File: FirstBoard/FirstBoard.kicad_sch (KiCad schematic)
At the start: 25 parts, among them J0 Battery, J1 MPU0, J10 MPU9, J11 MPU10, J12 MPU11, J13 MPU12, J14 OPEN, J2 MPU1, J3 MPU2, J4 MPU3, J5 MPU4, J6 MPU5, J7 MPU6, J8 MPU7, J9 MPU8, U1 ESP32-DEVKIT1-V1-JOAO

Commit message: Adding symbols, footprint and first pcb drawing
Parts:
- removed U1: ESP32-DEVKIT1-V1-JOAO, symbol ESP32-DEVKIT-V1:ESP32-DEVKIT1-V1-JOAO
- removed U?: LM2596-Board, symbol TCC_Library:LM2596-Board
- added U1: ESP32-DEVKIT1-V1-JOAO, TCC_FOOTPRINTS:MODULE_ESP32_DEVKIT_V1, symbol TCC_Library:ESP32-DEVKIT1-V1-JOAO
- added U2: LM2596-Board, TCC_FOOTPRINTS:LM2596_Board, symbol TCC_Library:LM2596-Board
- D0, D1, D2: footprint (none) -> Resistor_THT:R_Axial_DIN0204_L3.6mm_D1.6mm_P7.62mm_Horizontal
- J0: footprint (none) -> Connector_PinHeader_2.54mm:PinHeader_1x02_P2.54mm_Vertical
- J1: footprint (none) -> Connector_PinHeader_2.54mm:PinHeader_1x06_P2.54mm_Vertical
- J10, J11, J12, J13, J2, J3, J4, J5, J6, J7, J8, J9: footprint (none) -> Connector_PinHeader_2.54mm:PinHeader_1x05_P2.54mm_Vertical
- J14: footprint (none) -> Connector_PinHeader_2.54mm:PinHeader_2x04_P2.54mm_Vertical
- R0, R1: footprint (none) -> Resistor_THT:R_Axial_DIN0207_L6.3mm_D2.5mm_P10.16mm_Horizontal
- R2: renamed from R1; footprint (none) -> Resistor_THT:R_Axial_DIN0207_L6.3mm_D2.5mm_P10.16mm_Horizontal
- R3: renamed from R2; footprint (none) -> Resistor_THT:R_Axial_DIN0207_L6.3mm_D2.5mm_P10.16mm_Horizontal
- R4: renamed from R3; footprint (none) -> Resistor_THT:R_Axial_DIN0207_L6.3mm_D2.5mm_P10.16mm_Horizontal
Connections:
- net 3v3: now also U1.16 (3.3V), U2.3 (OUT+)
- net AD0_0: now also U1.12 (D12)
- net AD0_1: now also U1.11 (D14)
- net AD0_10: now also U1.21 (D16)
- net AD0_11: now also U1.22 (D17)
- net AD0_12: now also U1.23 (D5)
- net AD0_2: now also U1.10 (D27)
- net AD0_3: now also U1.9 (D26)
- net AD0_4: now also U1.8 (D25)
- net AD0_5: now also U1.7 (D33)
- net AD0_6: now also U1.6 (D32)
- net AD0_7: now also U1.18 (D15)
- net AD0_8: now also U1.19 (D2)
- net AD0_9: now also U1.20 (D4)
- net BAT+: now also U2.1 (IN+)
- net BAT-: now also U2.2 (IN-)
- net D1: now also U1.28 (D1)
- net GND: now also U1.14 (GND), U1.17 (GND), U2.4 (OUT-)
- net INT: now also U1.13 (D13)
- net LED_B: now also U1.27 (D3)
- net LED_G: now also U1.4 (D34)
- net LED_R: now also U1.5 (D25)
- net MISO: now also U1.25 (D19-MISO)
- net MOSI: now also U1.30 (D23-MOSI)
- net SCK: now also U1.24 (D18-SCK)
- net SCL: now also U1.29 (D22-SCL)
- net SDA: now also U1.26 (D21-SDA)
- net at J14.1 (Pin_1): now also U1.15 (VIN)
- net at J14.2 (Pin_2): now also U1.3 (VN)
- net at J14.3 (Pin_3): now also U1.2 (VP)
- net at J14.4 (Pin_4): now also U1.1 (EN)

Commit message: changing layour, adding SD card
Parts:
- removed D2: LED B, Resistor_THT:R_Axial_DIN0204_L3.6mm_D1.6mm_P7.62mm_Horizontal, symbol Device:LED
- removed J10: MPU9, Connector_PinHeader_2.54mm:PinHeader_1x05_P2.54mm_Vertical, symbol Connector_Generic:Conn_01x05
- removed J11: MPU10, Connector_PinHeader_2.54mm:PinHeader_1x05_P2.54mm_Vertical, symbol Connector_Generic:Conn_01x05
- removed J12: MPU11, Connector_PinHeader_2.54mm:PinHeader_1x05_P2.54mm_Vertical, symbol Connector_Generic:Conn_01x05
- removed J13: MPU12, Connector_PinHeader_2.54mm:PinHeader_1x05_P2.54mm_Vertical, symbol Connector_Generic:Conn_01x05
- removed J14: OPEN, Connector_PinHeader_2.54mm:PinHeader_2x04_P2.54mm_Vertical, symbol Connector_Generic:Conn_01x08
- removed J2: MPU1, Connector_PinHeader_2.54mm:PinHeader_1x05_P2.54mm_Vertical, symbol Connector_Generic:Conn_01x05
- removed J3: MPU2, Connector_PinHeader_2.54mm:PinHeader_1x05_P2.54mm_Vertical, symbol Connector_Generic:Conn_01x05
- removed J4: MPU3, Connector_PinHeader_2.54mm:PinHeader_1x05_P2.54mm_Vertical, symbol Connector_Generic:Conn_01x05
- removed J5: MPU4, Connector_PinHeader_2.54mm:PinHeader_1x05_P2.54mm_Vertical, symbol Connector_Generic:Conn_01x05
- removed J6: MPU5, Connector_PinHeader_2.54mm:PinHeader_1x05_P2.54mm_Vertical, symbol Connector_Generic:Conn_01x05
- removed J7: MPU6, Connector_PinHeader_2.54mm:PinHeader_1x05_P2.54mm_Vertical, symbol Connector_Generic:Conn_01x05
- removed J8: MPU7, Connector_PinHeader_2.54mm:PinHeader_1x05_P2.54mm_Vertical, symbol Connector_Generic:Conn_01x05
- removed J9: MPU8, Connector_PinHeader_2.54mm:PinHeader_1x05_P2.54mm_Vertical, symbol Connector_Generic:Conn_01x05
- removed R0, R1: 4k7, Resistor_THT:R_Axial_DIN0207_L6.3mm_D2.5mm_P10.16mm_Horizontal, symbol Device:R
- removed R4: 220R, Resistor_THT:R_Axial_DIN0207_L6.3mm_D2.5mm_P10.16mm_Horizontal, symbol Device:R
- added J10: MPU9, Connector_PinHeader_2.54mm:PinHeader_1x06_P2.54mm_Vertical, symbol Connector_Generic:Conn_01x06
- added J11: MPU10, Connector_PinHeader_2.54mm:PinHeader_1x06_P2.54mm_Vertical, symbol Connector_Generic:Conn_01x06
- added J12: MPU11, Connector_PinHeader_2.54mm:PinHeader_1x06_P2.54mm_Vertical, symbol Connector_Generic:Conn_01x06
- added J13: MPU12, Connector_PinHeader_2.54mm:PinHeader_1x06_P2.54mm_Vertical, symbol Connector_Generic:Conn_01x06
- added J14: Open, Connector_PinHeader_2.54mm:PinHeader_1x05_P2.54mm_Vertical, symbol Connector_Generic:Conn_01x05
- added J15: SD_CARD, Connector_PinHeader_2.54mm:PinHeader_1x06_P2.54mm_Vertical, symbol Connector_Generic:Conn_01x06
- added J2: MPU1, Connector_PinHeader_2.54mm:PinHeader_1x06_P2.54mm_Vertical, symbol Connector_Generic:Conn_01x06
- added J3, J4: MPU3, Connector_PinHeader_2.54mm:PinHeader_1x06_P2.54mm_Vertical, symbol Connector_Generic:Conn_01x06
- added J5: MPU4, Connector_PinHeader_2.54mm:PinHeader_1x06_P2.54mm_Vertical, symbol Connector_Generic:Conn_01x06
- added J6: MPU5, Connector_PinHeader_2.54mm:PinHeader_1x06_P2.54mm_Vertical, symbol Connector_Generic:Conn_01x06
- added J7: MPU6, Connector_PinHeader_2.54mm:PinHeader_1x06_P2.54mm_Vertical, symbol Connector_Generic:Conn_01x06
- added J8: MPU7, Connector_PinHeader_2.54mm:PinHeader_1x06_P2.54mm_Vertical, symbol Connector_Generic:Conn_01x06
- added J9: MPU8, Connector_PinHeader_2.54mm:PinHeader_1x06_P2.54mm_Vertical, symbol Connector_Generic:Conn_01x06
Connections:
- net D1 is gone; now on net AD0_6: U1.28 (D1)
- net LED_B is gone; now on net AD0_5: U1.27 (D3)
- net 3v3: now also J10.1 (Pin_1), J11.1 (Pin_1), J12.1 (Pin_1), J13.1 (Pin_1), J15.2 (Pin_2), J2.1 (Pin_1), J3.1 (Pin_1), J4.1 (Pin_1), J5.1 (Pin_1), J6.1 (Pin_1), J7.1 (Pin_1), J8.1 (Pin_1), J9.1 (Pin_1)
- net AD0_0: now also U1.18 (D15); no longer U1.12 (D12)
- net AD0_1: now also U1.19 (D2), J2.5 (Pin_5); no longer U1.11 (D14)
- net AD0_10: now also U1.8 (D25), J11.5 (Pin_5); no longer U1.21 (D16)
- net AD0_11: now also U1.9 (D26), J12.5 (Pin_5); no longer U1.22 (D17)
- net AD0_12: now also U1.10 (D27), J13.5 (Pin_5); no longer U1.23 (D5)
- net AD0_2: now also U1.20 (D4), J3.5 (Pin_5); no longer U1.10 (D27)
- net AD0_3: now also U1.21 (D16), J4.5 (Pin_5); no longer U1.9 (D26)
- net AD0_4: now also U1.22 (D17), J5.5 (Pin_5); no longer U1.8 (D25)
- net AD0_5: now also J6.5 (Pin_5); no longer U1.7 (D33)
- net AD0_6: now also J7.5 (Pin_5); no longer U1.6 (D32)
- net AD0_7: now also U1.4 (D34), J8.5 (Pin_5); no longer U1.18 (D15)
- net AD0_8: now also U1.6 (D32), J9.5 (Pin_5); no longer U1.19 (D2)
- net AD0_9: now also U1.7 (D33), J10.5 (Pin_5); no longer U1.20 (D4)
- net GND: now also J10.2 (Pin_2), J11.2 (Pin_2), J12.2 (Pin_2), J13.2 (Pin_2), J15.1 (Pin_1), J2.2 (Pin_2), J3.2 (Pin_2), J4.2 (Pin_2), J5.2 (Pin_2), J6.2 (Pin_2), J7.2 (Pin_2), J8.2 (Pin_2), J9.2 (Pin_2)
- net LED_G: now also U1.12 (D12); no longer U1.4 (D34)
- net LED_R: now also U1.11 (D14); no longer U1.5 (D25)
- net MISO: now also J15.3 (Pin_3)
- net MOSI: now also J15.4 (Pin_4)
- net SCK: now also J15.5 (Pin_5)
- net SCL: now also J1.3 (Pin_3), J10.3 (Pin_3), J11.3 (Pin_3), J12.3 (Pin_3), J13.3 (Pin_3), J2.3 (Pin_3), J3.3 (Pin_3), J4.3 (Pin_3), J5.3 (Pin_3), J6.3 (Pin_3), J7.3 (Pin_3), J8.3 (Pin_3), J9.3 (Pin_3); no longer J1.4 (Pin_4)
- net SDA: now also J1.4 (Pin_4), J10.4 (Pin_4), J11.4 (Pin_4), J12.4 (Pin_4), J13.4 (Pin_4), J2.4 (Pin_4), J3.4 (Pin_4), J4.4 (Pin_4), J5.4 (Pin_4), J6.4 (Pin_4), J7.4 (Pin_4), J8.4 (Pin_4), J9.4 (Pin_4); no longer J1.3 (Pin_3)
- net at U1.15 (VIN): now also J14.1 (Pin_1)
- net at U1.3 (VN): now also J14.3 (Pin_3)
- net at U1.2 (VP): now also J14.4 (Pin_4)
- net at U1.1 (EN): now also J14.5 (Pin_5)
- new net: J14.2 (Pin_2), U1.5 (D35)
- new net SS: J15.6 (Pin_6), U1.23 (D5)

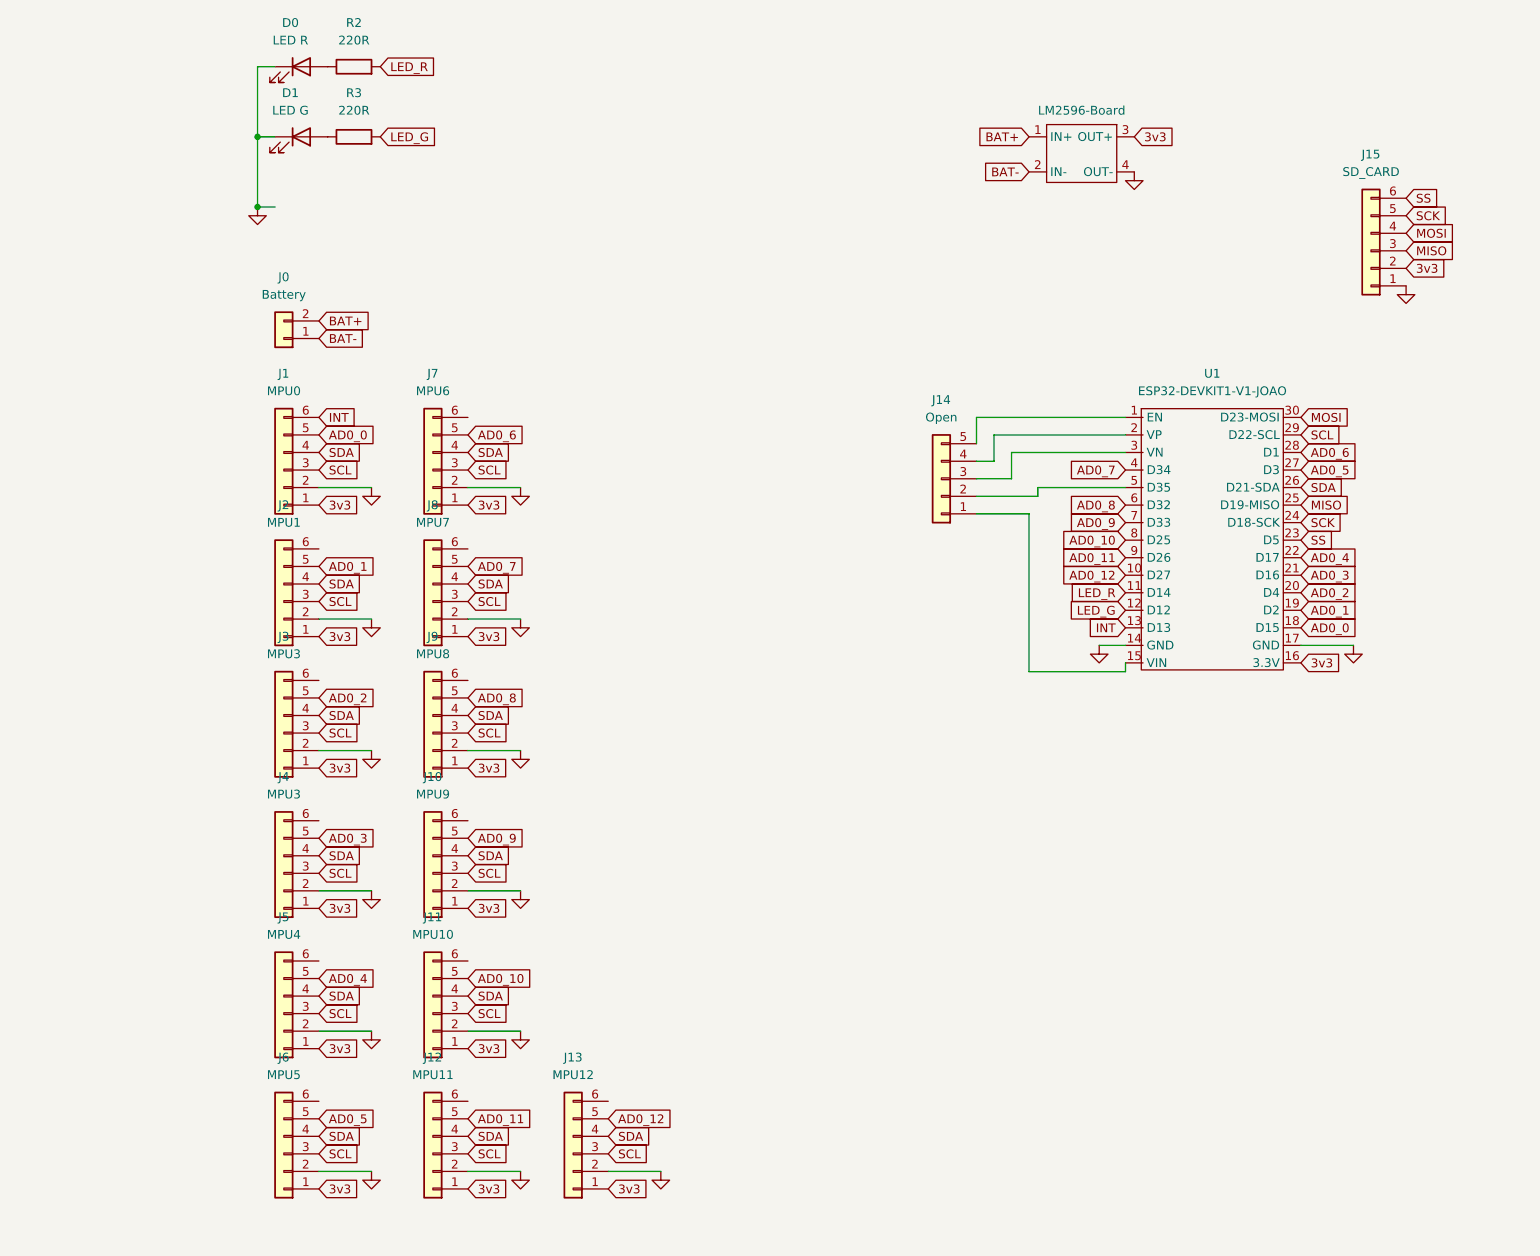
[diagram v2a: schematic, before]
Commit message: changing number of pins on MPU connector
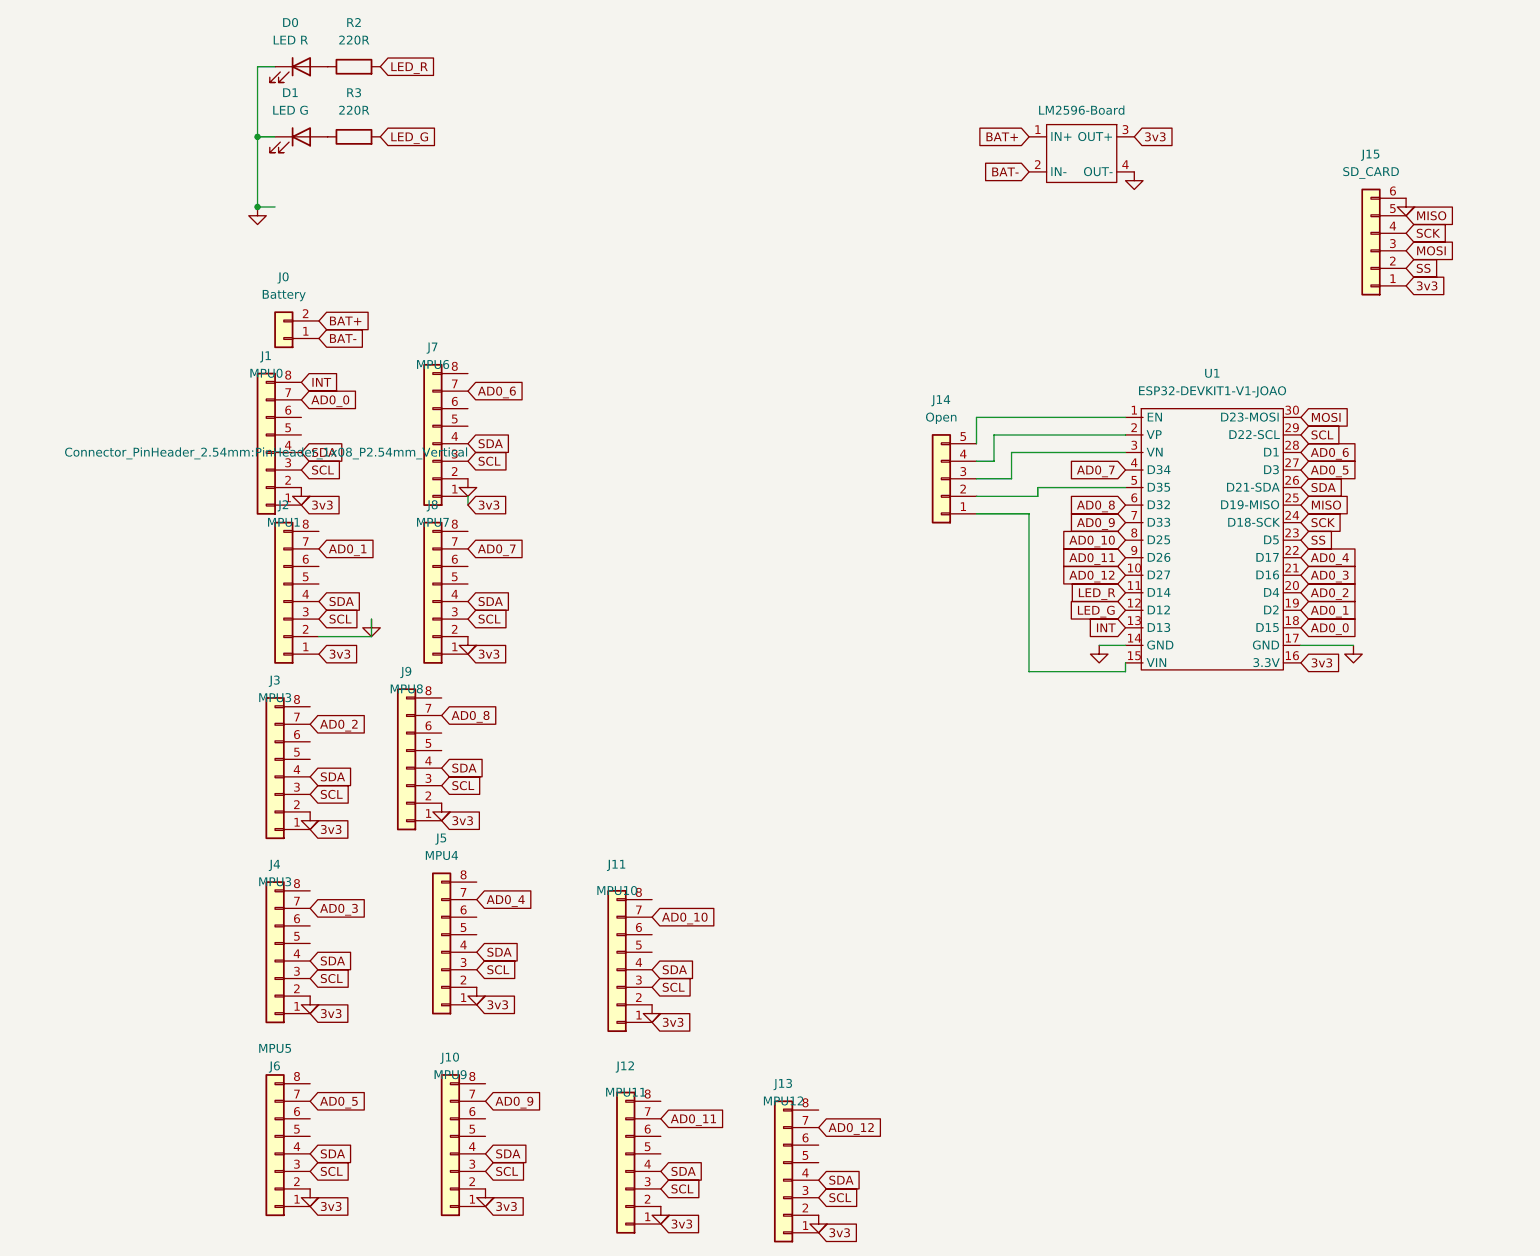
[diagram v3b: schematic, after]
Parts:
- J1, J10, J11, J12, J13, J2, J3, J4, J5, J6, J7, J8, J9: footprint Connector_PinHeader_2.54mm:PinHeader_1x06_P2.54mm_Vertical -> Connector_PinHeader_2.54mm:PinHeader_1x08_P2.54mm_Vertical; symbol Connector_Generic:Conn_01x06 -> Connector_Generic:Conn_01x08
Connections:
- net 3v3: now also J15.1 (Pin_1); no longer J15.2 (Pin_2)
- net AD0_0: now also J1.7 (Pin_7); no longer J1.5 (Pin_5)
- net AD0_1: now also J2.7 (Pin_7); no longer J2.5 (Pin_5)
- net AD0_10: now also J11.7 (Pin_7); no longer J11.5 (Pin_5)
- net AD0_11: now also J12.7 (Pin_7); no longer J12.5 (Pin_5)
- net AD0_12: now also J13.7 (Pin_7); no longer J13.5 (Pin_5)
- net AD0_2: now also J3.7 (Pin_7); no longer J3.5 (Pin_5)
- net AD0_3: now also J4.7 (Pin_7); no longer J4.5 (Pin_5)
- net AD0_4: now also J5.7 (Pin_7); no longer J5.5 (Pin_5)
- net AD0_5: now also J6.7 (Pin_7); no longer J6.5 (Pin_5)
- net AD0_6: now also J7.7 (Pin_7); no longer J7.5 (Pin_5)
- net AD0_7: now also J8.7 (Pin_7); no longer J8.5 (Pin_5)
- net AD0_8: now also J9.7 (Pin_7); no longer J9.5 (Pin_5)
- net AD0_9: now also J10.7 (Pin_7); no longer J10.5 (Pin_5)
- net GND: now also J15.6 (Pin_6); no longer J15.1 (Pin_1)
- net INT: now also J1.8 (Pin_8); no longer J1.6 (Pin_6)
- net MISO: now also J15.5 (Pin_5); no longer J15.3 (Pin_3)
- net MOSI: now also J15.3 (Pin_3); no longer J15.4 (Pin_4)
- net SCK: now also J15.4 (Pin_4); no longer J15.5 (Pin_5)
- net SS: now also J15.2 (Pin_2); no longer J15.6 (Pin_6)
